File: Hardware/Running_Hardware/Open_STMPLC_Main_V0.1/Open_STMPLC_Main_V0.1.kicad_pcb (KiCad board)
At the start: 4 copper layers, 168.8 x 90 mm, 181 parts, among them J1 Conn_02x08_Odd_Even, J10 10144518-041802LF, J12 USB C, J13 RJ45_Hanrun_HR911105A_Horizon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, J2 USB C, J3 Conn_01x04, J4 TF-01A, J5 Conn_Coaxial, J6 Conn_Coaxial, J7 Simcard_Nano, J8 10144518-041802LF, J9 10144518-041802LF, Q1 DTC143Z, Q2 DTC143Z, Q3 DTC143Z, Q4 DTC143Z, Q5 DTC143Z, Q6 DTC143Z, Q7 DTC143Z, Q8 DTC143Z, SW1 Switch_6x6, SW2 SW_DIP_x01, SW3 Switch_6x6, U1 STM32F407IGTx, U10 AP63205WU, U2 ADM2587E, U3 TPS3430WDRC, U4 CH340C, U5 AMS1117-3.3, U6 W25Q64JVSSIQ, U7 LAN8720A, U8 EC200U, U9 AP63200WU, Y1 48MHz, Y2 32.768kHz, Y3 25MHz

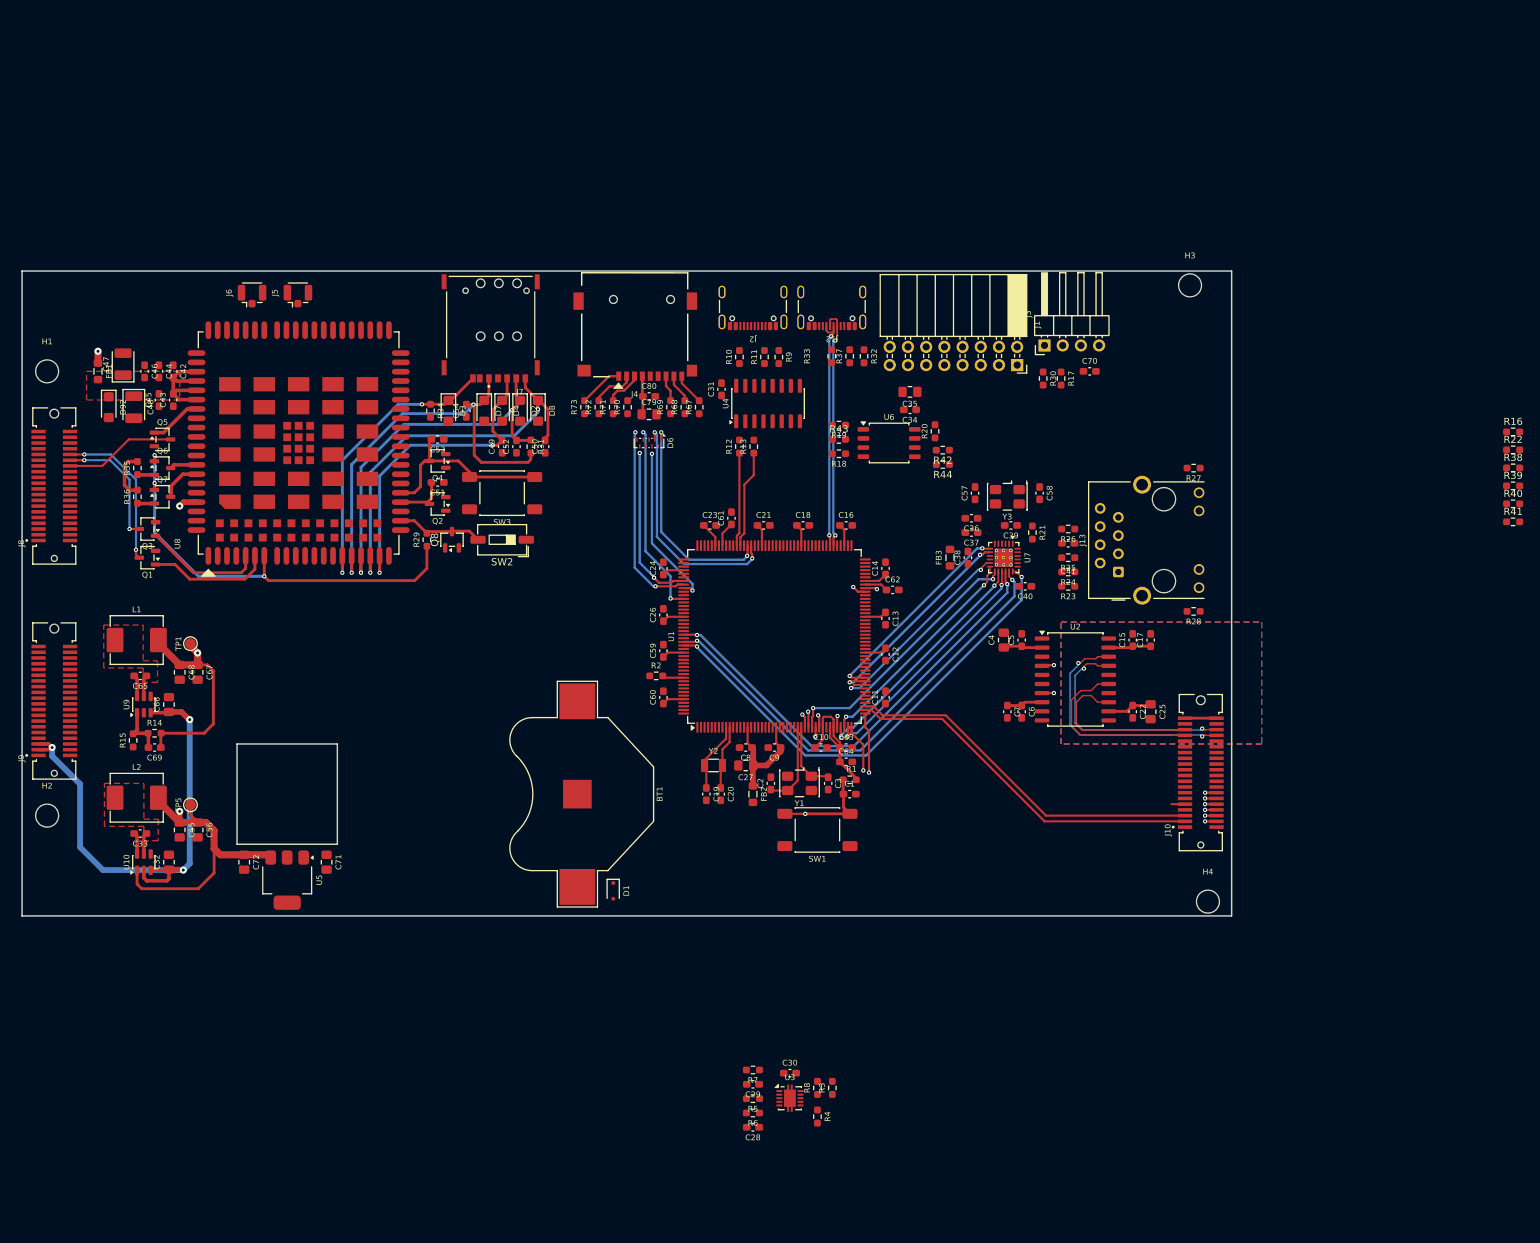
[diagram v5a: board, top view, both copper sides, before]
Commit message: Pin mapping - MCU connectors
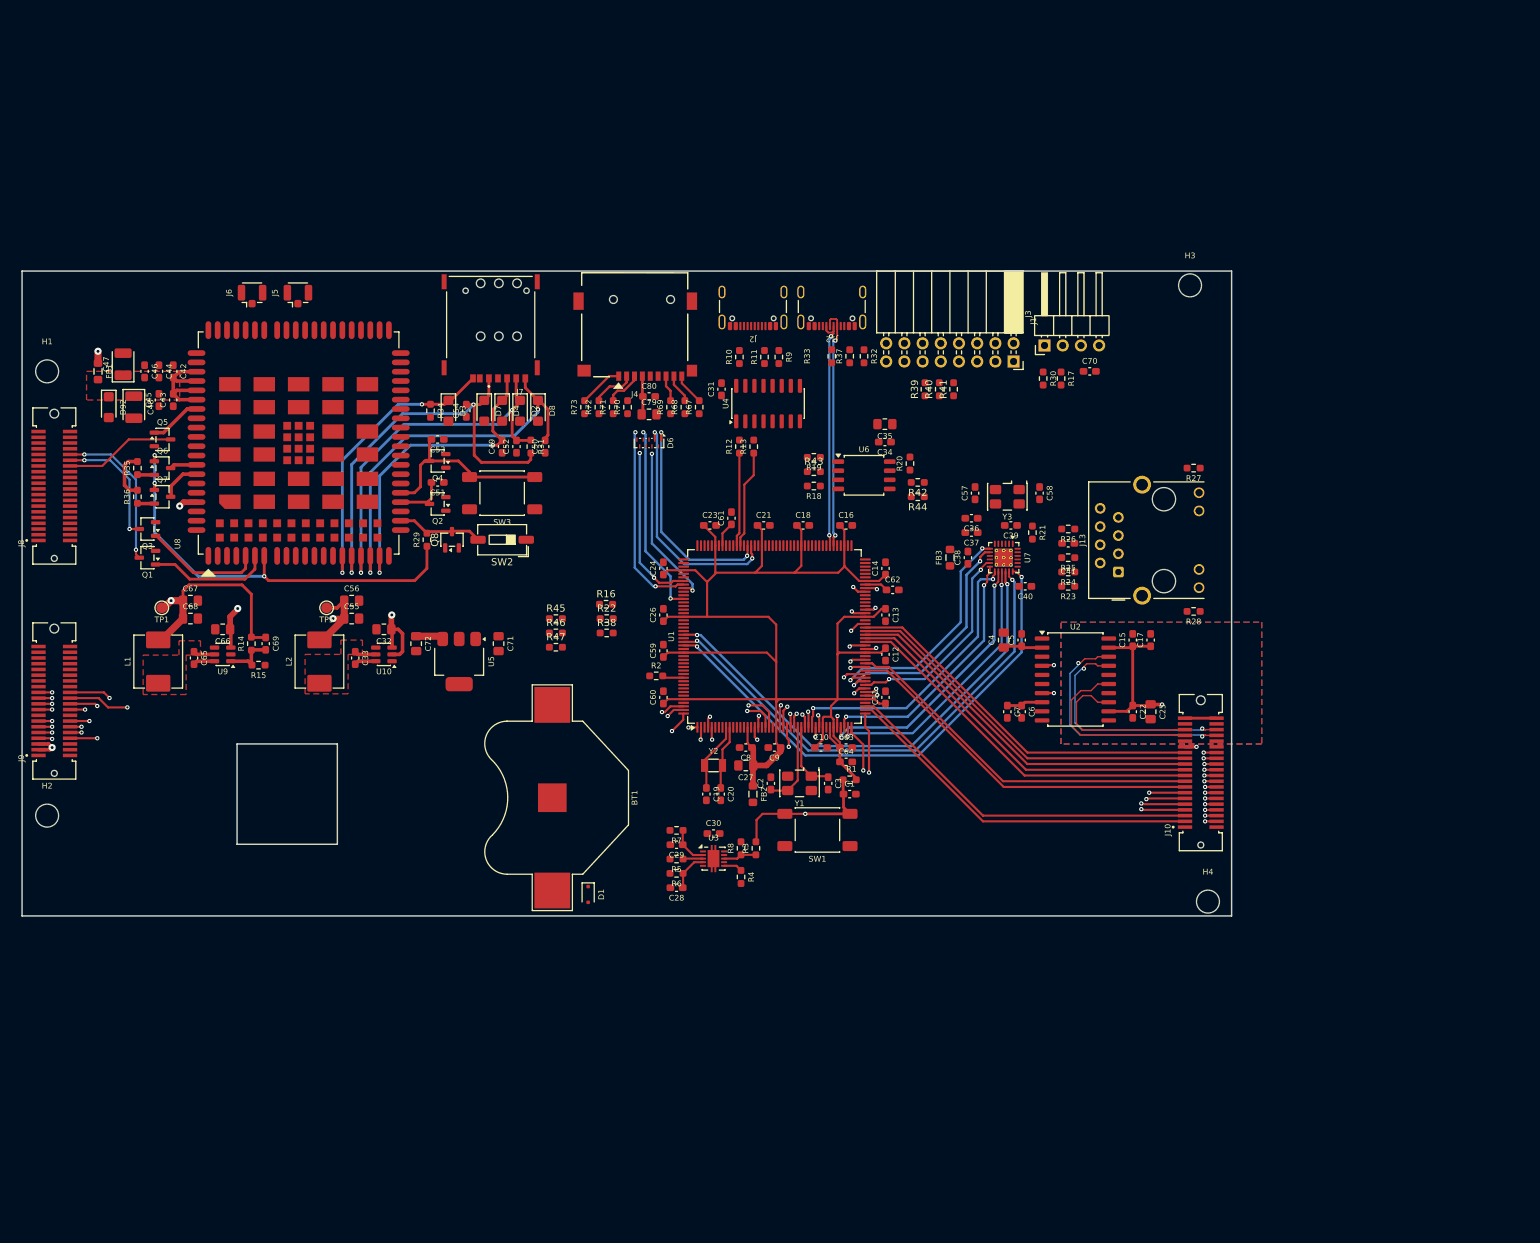
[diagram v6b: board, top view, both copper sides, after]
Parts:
- added R45: 0R, Resistor_SMD:R_0603_1608Metric_Pad0.98x0.95mm_HandSolder, F.Cu at (124.5, 98.5)
- added R46: 0R, Resistor_SMD:R_0603_1608Metric_Pad0.98x0.95mm_HandSolder, F.Cu at (124.5, 100.5)
- added R47: 0R, Resistor_SMD:R_0603_1608Metric_Pad0.98x0.95mm_HandSolder, F.Cu at (124.5, 102.5)
- moved R16 128.9 mm to (131.5, 96.5)
- moved R22 128.7 mm to (131.6, 98.5)
- moved R38 128.6 mm to (131.6, 100.5)
- moved R39 83.2 mm to (176.0, 66.5), turned to 90 degrees
- moved R40 81.7 mm to (178.0, 66.5), turned to 90 degrees
- moved R41 80.2 mm to (180.0, 66.5), turned to 90 degrees
- moved U10 44.3 mm to (100.5, 103.5), turned to 180 degrees
- moved C32 44.2 mm to (100.5, 100.0), turned to 180 degrees
- moved C71 38.8 mm to (116.5, 102.0)
- moved C72 38.8 mm to (105.0, 102.0)
- moved U5 38.8 mm to (111.0, 104.5)
- moved C33 38.7 mm to (96.5, 104.0), turned to -90 degrees
- moved C56 38.6 mm to (96.0, 96.0), turned to 0 degrees
- moved C55 38.0 mm to (96.0, 98.5), turned to 0 degrees
- moved C28 35.1 mm to (141.3, 136.1)
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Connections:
- U1 pad 1: unconnected-(U1-PE2-Pad1) -> /B2B_Connector/DIG_HS_~{SHDN}_4
- U1 pad 17: unconnected-(U1-PF1-Pad17) -> /B2B_Connector/DIG_HS_~{SHDN}_2
- U1 pad 174: unconnected-(U1-PI5-Pad174) -> /B2B_Connector/DIG_HS_~{FAULT}_4
- U1 pad 175: unconnected-(U1-PI6-Pad175) -> /B2B_Connector/DIG_HS_~{FAULT}_3
- U1 pad 176: unconnected-(U1-PI7-Pad176) -> /B2B_Connector/DIG_HS_OUT_3
- U1 pad 18: unconnected-(U1-PF2-Pad18) -> /B2B_Connector/DIG_HS_~{FAULT}_2
- U1 pad 2: unconnected-(U1-PE3-Pad2) -> /B2B_Connector/DIG_HS_~{SHDN}_3
- U1 pad 20: unconnected-(U1-PF4-Pad20) -> /B2B_Connector/DIG_HS_IMON_4
- U1 pad 21: unconnected-(U1-PF5-Pad21) -> /B2B_Connector/DIG_HS_IMON_3
- U1 pad 24: unconnected-(U1-PF6-Pad24) -> /B2B_Connector/DIG_HS_OUT_1
- U1 pad 25: unconnected-(U1-PF7-Pad25) -> /B2B_Connector/DIG_HS_~{FAULT}_1
- U1 pad 26: unconnected-(U1-PF8-Pad26) -> /B2B_Connector/DIG_HS_IMON_1
- U1 pad 27: unconnected-(U1-PF9-Pad27) -> /B2B_Connector/DIG_HS_IMON_2
- U1 pad 28: unconnected-(U1-PF10-Pad28) -> /B2B_Connector/DIG_HS_~{SHDN}_1
- U1 pad 4: unconnected-(U1-PE5-Pad4) -> /B2B_Connector/DIG_HS_OUT_4
- U1 pad 48: unconnected-(U1-BYPASS_REG-Pad48) -> GND
- U1 pad 5: unconnected-(U1-PE6-Pad5) -> /B2B_Connector/DIG_HS_OUT_2
- U1 pad 50: unconnected-(U1-PA4-Pad50) -> /B2B_Connector/DIG_OUT_7
- U1 pad 51: unconnected-(U1-PA5-Pad51) -> /B2B_Connector/DIG_OUT_~{FAULT}_6
- U1 pad 52: unconnected-(U1-PA6-Pad52) -> /B2B_Connector/DIG_OUT_DIAG_6
- U1 pad 56: unconnected-(U1-PB0-Pad56) -> /B2B_Connector/DIG_OUT_6
- U1 pad 57: unconnected-(U1-PB1-Pad57) -> /B2B_Connector/RUN_LED
- U1 pad 58: unconnected-(U1-PB2-Pad58) -> /B2B_Connector/FAULT_LED
- U1 pad 59: unconnected-(U1-PF11-Pad59) -> /B2B_Connector/DIG_OUT_~{FAULT}_4
- U1 pad 60: unconnected-(U1-PF12-Pad60) -> /B2B_Connector/DIG_OUT_~{FAULT}_3
- U1 pad 63: unconnected-(U1-PF13-Pad63) -> /B2B_Connector/DIG_OUT_DIAG_3
- U1 pad 64: unconnected-(U1-PF14-Pad64) -> /B2B_Connector/DIG_OUT_3
- U1 pad 65: unconnected-(U1-PF15-Pad65) -> /B2B_Connector/DIG_OUT_DIAG_4
- U1 pad 66: unconnected-(U1-PG0-Pad66) -> /B2B_Connector/DIG_OUT_4
- U1 pad 67: unconnected-(U1-PG1-Pad67) -> /B2B_Connector/DIG_OUT_2
- U1 pad 68: unconnected-(U1-PE7-Pad68) -> /B2B_Connector/DIG_OUT_DIAG_2
- U1 pad 69: unconnected-(U1-PE8-Pad69) -> /B2B_Connector/DIG_OUT_~{FAULT}_2
- U1 pad 70: unconnected-(U1-PE9-Pad70) -> /B2B_Connector/DIG_OUT_1
- U1 pad 73: unconnected-(U1-PE10-Pad73) -> /B2B_Connector/DIG_OUT_DIAG_1
- U1 pad 74: unconnected-(U1-PE11-Pad74) -> /B2B_Connector/DIG_OUT_~{FAULT}_1
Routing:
- net /Microcontroller/3V3_MCU: track 70.6 -> 210.4 mm
- net /B2B_Connector/DIG_HS_~{SHDN}_1: track 0.00 -> 137.6 mm, vias 0 -> 2
- net /B2B_Connector/DIG_HS_~{FAULT}_1: track 0.00 -> 137.3 mm, vias 0 -> 2
- net /B2B_Connector/DIG_HS_OUT_1: track 0.00 -> 136.2 mm, vias 0 -> 2
- net /B2B_Connector/DIG_HS_IMON_2: track 0.00 -> 133.8 mm, vias 0 -> 2
- net /B2B_Connector/DIG_HS_IMON_1: track 0.00 -> 132.4 mm, vias 0 -> 2
- net /B2B_Connector/DIG_HS_~{FAULT}_2: track 0.00 -> 126.1 mm, vias 0 -> 2
- net /B2B_Connector/DIG_HS_~{SHDN}_2: track 0.00 -> 120.0 mm, vias 0 -> 2
- net /B2B_Connector/DIG_HS_OUT_4: track 0.00 -> 115.8 mm, vias 0 -> 2
- net /B2B_Connector/DIG_HS_OUT_2: track 0.00 -> 113.4 mm, vias 0 -> 2
- net /B2B_Connector/DIG_HS_IMON_3: track 0.00 -> 105.5 mm, vias 0 -> 2
- net /B2B_Connector/DIG_HS_IMON_4: track 0.00 -> 99.7 mm, vias 0 -> 2
- net /B2B_Connector/DIG_HS_~{SHDN}_3: track 0.00 -> 97.5 mm, vias 0 -> 2
- net /B2B_Connector/DIG_HS_OUT_3: track 0.00 -> 93.3 mm, vias 0 -> 2
- net /B2B_Connector/DIG_HS_~{FAULT}_3: track 0.00 -> 91.9 mm, vias 0 -> 2
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
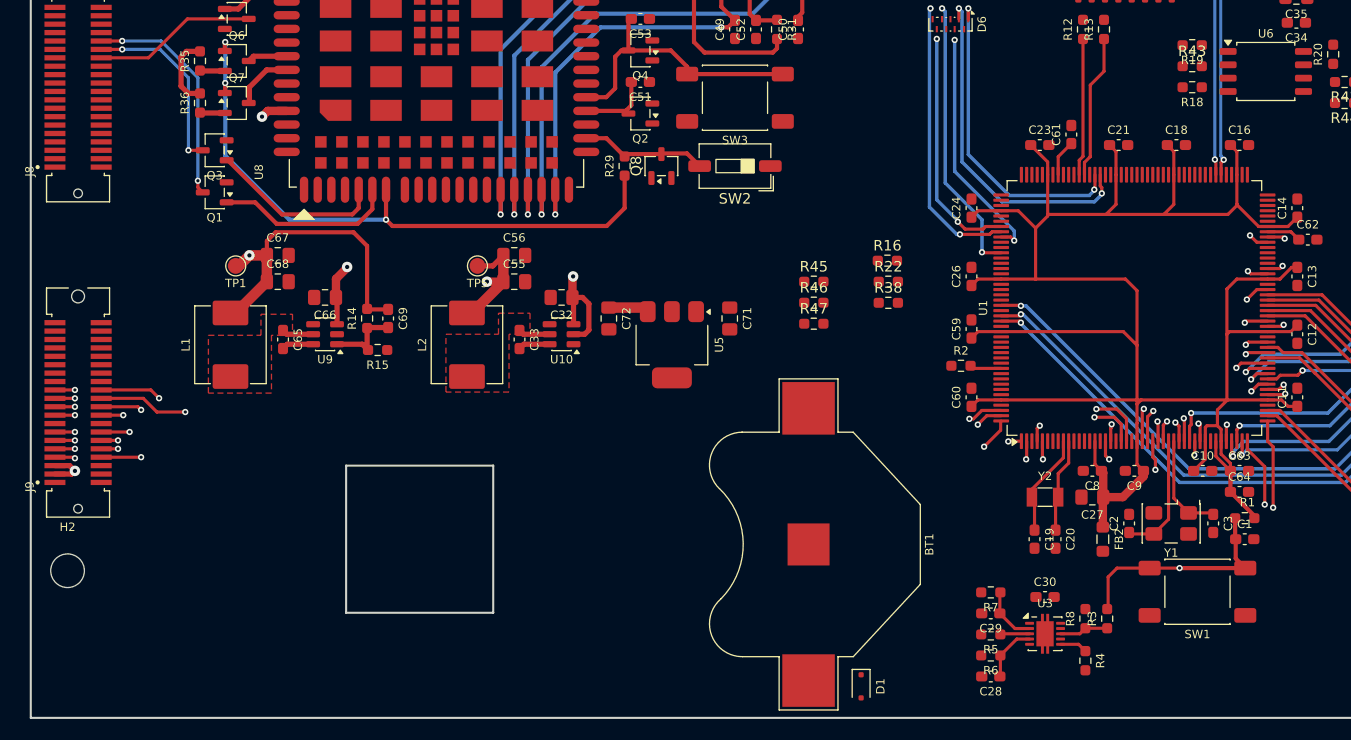
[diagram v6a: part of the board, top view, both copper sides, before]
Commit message: Pin mapping
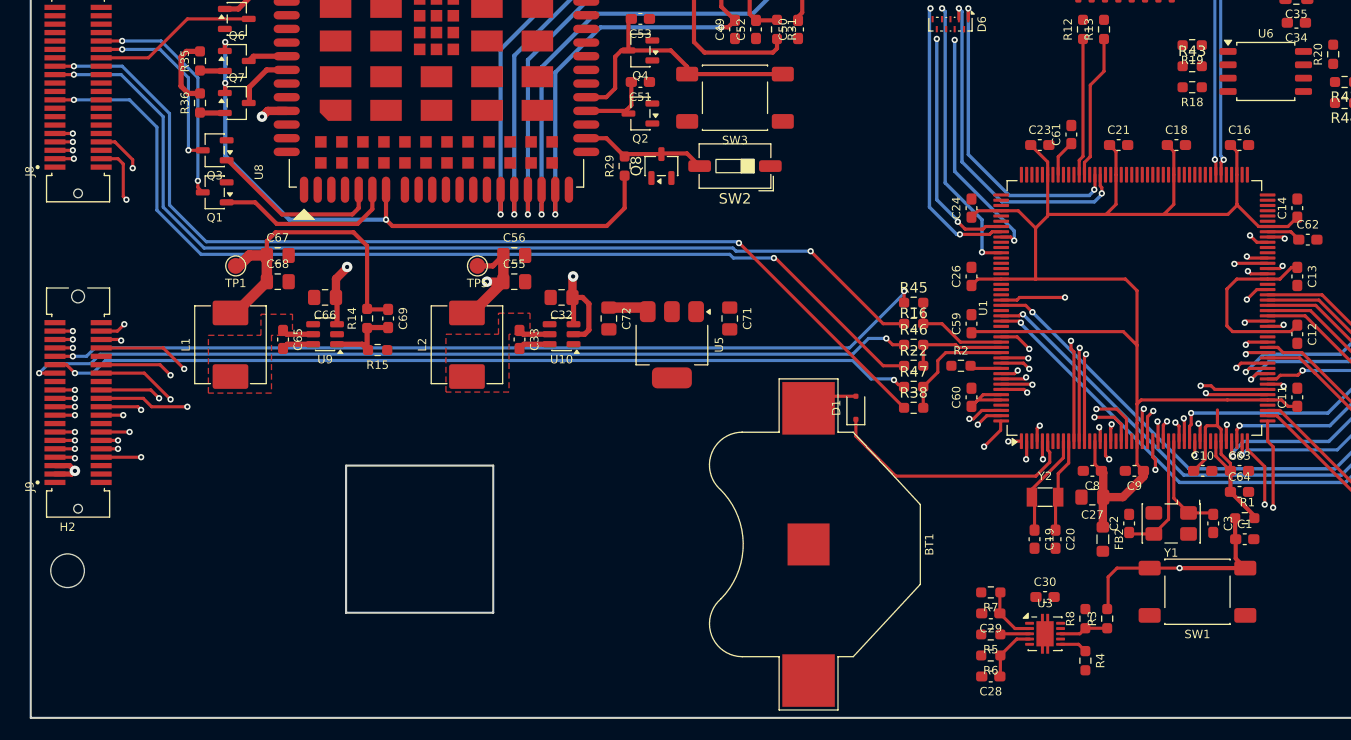
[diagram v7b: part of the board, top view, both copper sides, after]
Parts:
- moved D1 26.5 mm to (128.5, 110.5), turned to 90 degrees
- moved R47 11.2 mm to (134.0, 108.5)
- moved R46 10.3 mm to (134.0, 104.5)
- moved R38 10.3 mm to (134.0, 110.5)
- moved R45 9.71 mm to (134.0, 100.5)
- moved R22 8.36 mm to (134.0, 106.5)
- moved R16 6.50 mm to (134.0, 102.5)
- moved C59 0.50 mm to (139.5, 102.5)
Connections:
- R39 pad 1: /Microcontroller/SPI1_CLK -> /Microcontroller/SPI2_CLK
- R40 pad 1: /Microcontroller/SPI1_MISO -> /Microcontroller/SPI2_MISO
- R41 pad 1: /Microcontroller/SPI1_MOSI -> /Microcontroller/SPI2_MOSI
- R42 pad 1: /Microcontroller/SPI1_CLK -> /Microcontroller/SPI2_CLK
- R43 pad 1: /Microcontroller/SPI1_MISO -> /Microcontroller/SPI2_MISO
- R44 pad 1: /Microcontroller/SPI1_MOSI -> /Microcontroller/SPI2_MOSI
- U1 pad 11: unconnected-(U1-PI9-Pad11) -> /B2B_Connector/AOUT_M1_1
- U1 pad 12: unconnected-(U1-PI10-Pad12) -> /B2B_Connector/AOUT_M2_1
- U1 pad 13: unconnected-(U1-PI11-Pad13) -> /B2B_Connector/AOUT_~{OD}_1
- U1 pad 132: /Microcontroller/SPI1_CLK -> /Microcontroller/SPI2_CLK
- U1 pad 133: /Microcontroller/SPI1_MISO -> /Microcontroller/SPI2_MISO
- U1 pad 134: /Microcontroller/SPI1_MOSI -> /Microcontroller/SPI2_MOSI
- U1 pad 153: unconnected-(U1-PG10-Pad153) -> /B2B_Connector/AOUT_M2_2
- U1 pad 16: unconnected-(U1-PF0-Pad16) -> /B2B_Connector/ANALOG_IN_CS
- U1 pad 160: unconnected-(U1-PG15-Pad160) -> /B2B_Connector/DIG_IN_9
- U1 pad 164: unconnected-(U1-PB6-Pad164) -> /B2B_Connector/DIG_IN_12
- U1 pad 165: unconnected-(U1-PB7-Pad165) -> /B2B_Connector/DIG_IN_8
- U1 pad 167: unconnected-(U1-PB8-Pad167) -> /B2B_Connector/DIG_IN_11
- U1 pad 168: unconnected-(U1-PB9-Pad168) -> /B2B_Connector/DIG_IN_7
- U1 pad 169: unconnected-(U1-PE0-Pad169) -> /B2B_Connector/DIG_IN_10
- U1 pad 170: unconnected-(U1-PE1-Pad170) -> /B2B_Connector/ANALOG_IN_ERROR
- U1 pad 171: unconnected-(U1-PDR_ON-Pad171) -> /Microcontroller/3V3_MCU
- U1 pad 50: /B2B_Connector/DIG_OUT_7 -> /B2B_Connector/AOUT_VIN_1
- U1 pad 51: /B2B_Connector/DIG_OUT_~{FAULT}_6 -> /B2B_Connector/AOUT_VIN_2
- U1 pad 75: unconnected-(U1-PE12-Pad75) -> /B2B_Connector/DIG_OUT_~{FAULT}_6
- U1 pad 76: unconnected-(U1-PE13-Pad76) -> /B2B_Connector/DIG_OUT_7
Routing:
- net /B2B_Connector/AOUT_VIN_1: track 0.00 -> 124.7 mm, vias 0 -> 2
- net /B2B_Connector/AOUT_VIN_2: track 0.00 -> 121.9 mm, vias 0 -> 2
- net /B2B_Connector/AOUT_~{OD}_1: track 0.00 -> 117.6 mm, vias 0 -> 2
- net /B2B_Connector/AOUT_M2_1: track 0.00 -> 116.4 mm, vias 0 -> 2
- net /B2B_Connector/AOUT_M1_1: track 0.00 -> 113.8 mm, vias 0 -> 2
- net /B2B_Connector/AOUT_M2_2: track 0.00 -> 105.4 mm, vias 0 -> 2
- net /B2B_Connector/TEMP_MOSI: track 0.00 -> 99.3 mm, vias 0 -> 2
- net /B2B_Connector/ANALOG_IN_CS: track 0.00 -> 98.6 mm, vias 0 -> 2
- net /B2B_Connector/DIG_IN_10: track 0.00 -> 97.6 mm, vias 0 -> 2
- net /B2B_Connector/DIG_IN_12: track 0.00 -> 96.3 mm, vias 0 -> 2
- net /B2B_Connector/TEMP_MISO: track 0.00 -> 95.9 mm, vias 0 -> 2
- net /B2B_Connector/TEMP_SCLK: track 0.00 -> 95.6 mm, vias 0 -> 2
- net /B2B_Connector/DIG_IN_11: track 0.00 -> 94.5 mm, vias 0 -> 2
- net /B2B_Connector/DIG_IN_9: track 0.00 -> 92.7 mm, vias 0 -> 2
- net /B2B_Connector/DIG_IN_8: track 0.00 -> 92.4 mm, vias 0 -> 2
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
